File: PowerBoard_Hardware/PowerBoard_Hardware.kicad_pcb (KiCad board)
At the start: 4 copper layers, 279.4 x 127 mm, 152 parts, among them Q1 BSS138PW.115, Q10 Q_NMOS_GDS, Q11 Q_NMOS_GDS, Q12 Q_NMOS_GDS, Q13 Q_NMOS_GDS, Q2 BSS138PW.115, Q3 IPT020N10N3, Q4 IPT020N10N3, Q5 IPT020N10N3, Q6 Q_NMOS_GDS, Q7 Q_NMOS_GDS, Q8 Q_NMOS_GDS, Q9 Q_NMOS_GDS, U1 TM4C129E_Launchpad, U10 OKI, U11 LT1910, U12 LT1910, U13 LT1910, U14 LT1910, U15 ATC_FUSE_BLOCK, U16 ATC_FUSE_BLOCK, U17 ATC_FUSE_BLOCK, U18 ATC_FUSE_BLOCK, U19 ACS722xLCTR-40AU, U2 ATC_FUSE_BLOCK, U20 ACS722xLCTR-40AU, U21 ACS722xLCTR-40AU, U22 ACS722xLCTR-40AU, U23 LT1910, U24 LT1910, U25 LT1910, U26 LT1910, U27 ATC_FUSE_BLOCK, U28 ATC_FUSE_BLOCK, U29 ATC_FUSE_BLOCK, U3 ATC_FUSE_BLOCK, U30 ATC_FUSE_BLOCK, U31 ACS722xLCTR-40AU, U32 ACS722xLCTR-40AU, U33 ACS722xLCTR-40AU, U34 ACS722xLCTR-40AU, U4 ATC_FUSE_BLOCK, U5 LT1910, U6 LT1910, U7 ACS722xLCTR-40AU, U8 ACS722xLCTR-40AU, U9 ACS722xLCTR-40AU

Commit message: Moved Packages and Devices. Performed Basic Touch ups
Fixed some silkscreen and bad routing for a cleaner look. Moved the Packages and Devices to their own folder.
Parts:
- removed the Britt at (144.8, 55.9)
- removed the Carol at (196.8, 55.9)
- removed the G*** at (92.7, 48.9)
- added Britt: DC-DC_Converter, DC_DC_Converter_Quarter_Brick:DC_DC_Converter_Quarter_Brick, F.Cu at (144.8, 56.4)
- added Carol: DC-DC_Converter, DC_DC_Converter_Quarter_Brick:DC_DC_Converter_Quarter_Brick, F.Cu at (197.1, 55.4)
- added D14: D_Schottky, Diodes_SMD:D_0603, F.Cu at (105.4, 30.5)
- added G***: LOGO, MRDT-Silkscreen:MRDT_Logo_30mm, F.Cu at (118.4, 103.6)
- moved G*** 64.0 mm to (116.8, 89.9)
- moved D10 7.96 mm to (31.8, 103.5)
- moved D9 7.67 mm to (31.8, 120.0)
- moved D11 7.59 mm to (31.9, 87.0)
- moved D8 6.98 mm to (31.8, 138.4)
- moved D4 2.62 mm to (279.4, 50.8)
- moved D5 1.42 mm to (279.4, 125.7)
- moved D7 1.27 mm to (280.0, 101.0)
- moved D6 1.27 mm to (280.0, 74.3)
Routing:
- net +3.3VA: track 626.9 -> 646.8 mm, vias 14 -> 13
- net AUX_CTL: track 24.8 -> 7.21 mm
- net GND: track 231.2 -> 224.1 mm
- net COM_CTL: track 145.3 -> 139.1 mm
- net Net-(D8-Pad2): track 8.90 -> 4.10 mm
- net Net-(D11-Pad2): track 7.32 -> 2.61 mm
- net Net-(D9-Pad2): track 7.32 -> 3.32 mm
- net Net-(D10-Pad2): track 7.32 -> 3.95 mm
- net Net-(C29-Pad1): track 12.7 -> 16.0 mm
- net Net-(D4-Pad2): track 6.12 -> 3.32 mm
- net Net-(D5-Pad2): track 5.48 -> 3.95 mm
- net Net-(D7-Pad2): track 5.22 -> 3.95 mm
- net Net-(D6-Pad2): track 2.68 -> 3.95 mm
- net Net-(CONV1-Pad2): track 58.3 -> 59.3 mm
- net COM_IMEAS: track 124.1 -> 123.2 mm
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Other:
- board text added: "ACT"
- board text added: "COMM"
- board text added: "LOGIC"
- board text added: "Power Board Rev 1 2019 Mars Rover Design Team Missouri S&T Evan Hite"
- board text removed: "Actuation Bus"
- board text removed: "Communication Bus"
- board text removed: "Logic Bus"
- board text removed: "Power Board Rev 1 2019 Mars Rover Design Team Missouri University of Science and Technology Evan Hite"

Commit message: Corrected Vertical Anderson Package
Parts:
- removed Britt, Carol: DC-DC_Converter, DC_DC_Converter_Quarter_Brick:DC_DC_Converter_Quarter_Brick
- added CONV1: DC-DC_Converter, PowerBoard_Hardware:DC_DC_Converter_Quarter_Brick, F.Cu at (144.8, 56.4)
- added CONV2: DC-DC_Converter, PowerBoard_Hardware:DC_DC_Converter_Quarter_Brick, F.Cu at (197.1, 55.4)
- Conn1, Conn2, Conn3: footprint Vertical Anderson Double:Vertical Anderson Double -> PowerBoard_Hardware:Vertical_Anderson_Double_SidebySide
- moved Conn1 41.4 mm to (263.5, -10.8)
- moved Conn2 39.1 mm to (179.3, -8.51)
- moved Conn3 38.8 mm to (223.9, -8.26)

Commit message: Corrected Vertical Anderson Package and Replaced on Layout
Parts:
- moved Conn1 24.5 mm to (267.0, 13.5)
- moved Conn2 22.0 mm to (180.6, 13.5)
- moved Conn3 21.7 mm to (223.8, 13.5)
- moved D1 0.76 mm to (263.7, 17.8)
- moved R7 0.76 mm to (263.7, 23.3)
- moved REF** 0.25 mm to (279.7, 17.1)
- moved REF** 0.25 mm to (279.7, 83.8)

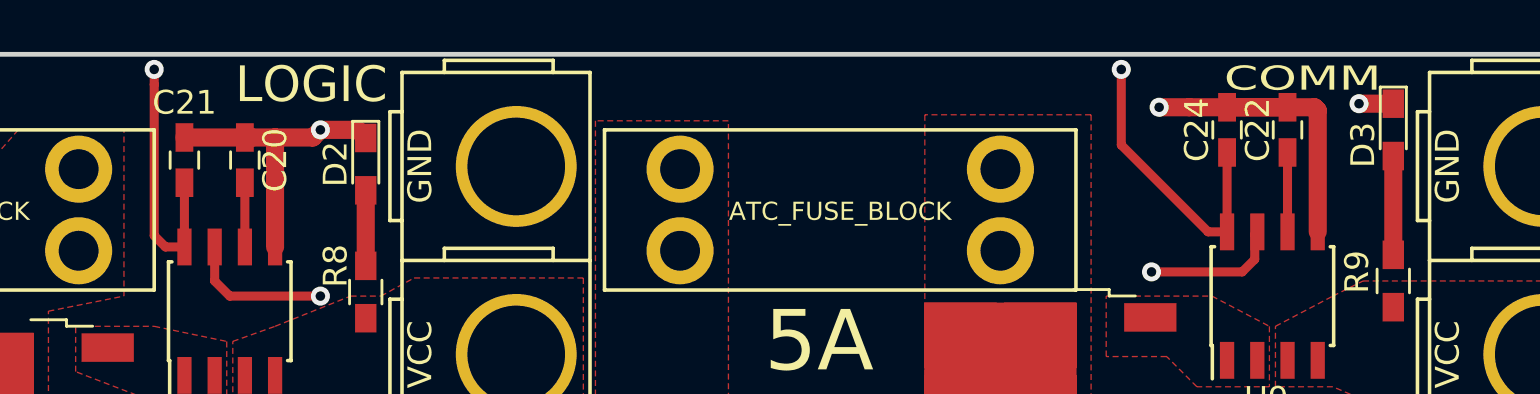
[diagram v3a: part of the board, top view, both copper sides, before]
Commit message: Swapped Placment of Comm & Logic Busses
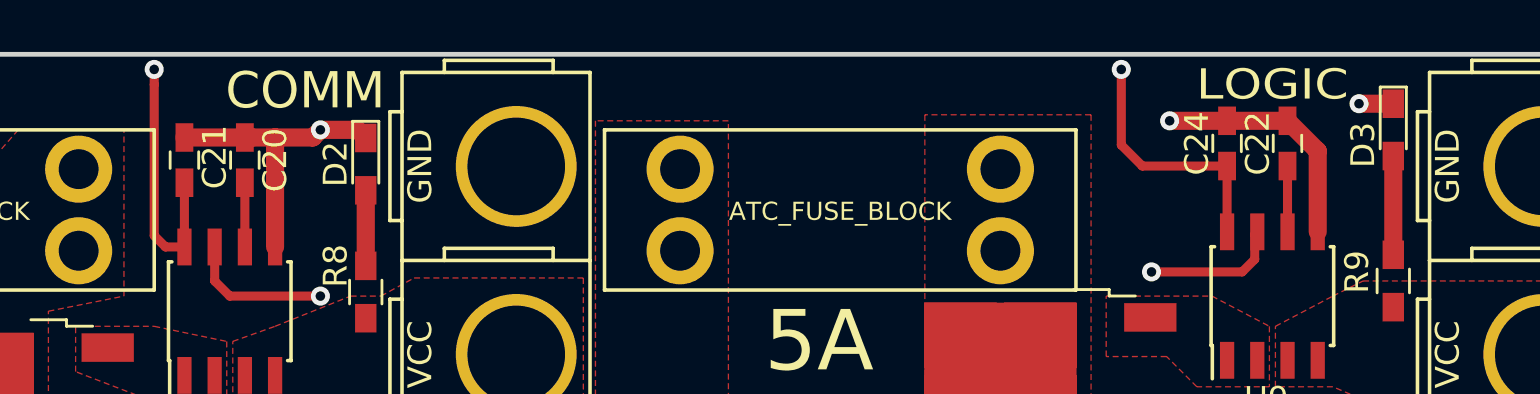
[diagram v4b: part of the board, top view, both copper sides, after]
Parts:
- moved C22 0.57 mm to (217.8, 16.4)
- moved C24 0.57 mm to (215.3, 16.4)
- turned C21 to 90 degrees
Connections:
- C21 pad 1: GND -> +3.3VA
- C21 pad 2: +3.3VA -> GND
- U1 pad PD1: COM_CTL -> LOGIC_CTL
- U1 pad PE0: LOGIC_IMEAS -> COM_IMEAS
- U1 pad PE1: COM_IMEAS -> LOGIC_IMEAS
- U1 pad PH2: LOGIC_CTL -> COM_CTL
- U5 pad 4: LOGIC_CTL -> COM_CTL
- U6 pad 4: COM_CTL -> LOGIC_CTL
- U7 pad 7: LOGIC_IMEAS -> COM_IMEAS
- U9 pad 7: COM_IMEAS -> LOGIC_IMEAS
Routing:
- net LOGIC_CTL: track 94.5 -> 139.1 mm, vias 1 -> 3
- net COM_CTL: track 139.1 -> 94.5 mm, vias 3 -> 1
- net LOGIC_IMEAS: track 90.4 -> 123.2 mm
- net COM_IMEAS: track 123.2 -> 90.4 mm
- net GND: track 224.1 -> 219.9 mm
- net +3.3VA: track 646.8 -> 645.0 mm
- net Net-(C22-Pad1): track 3.34 -> 2.77 mm

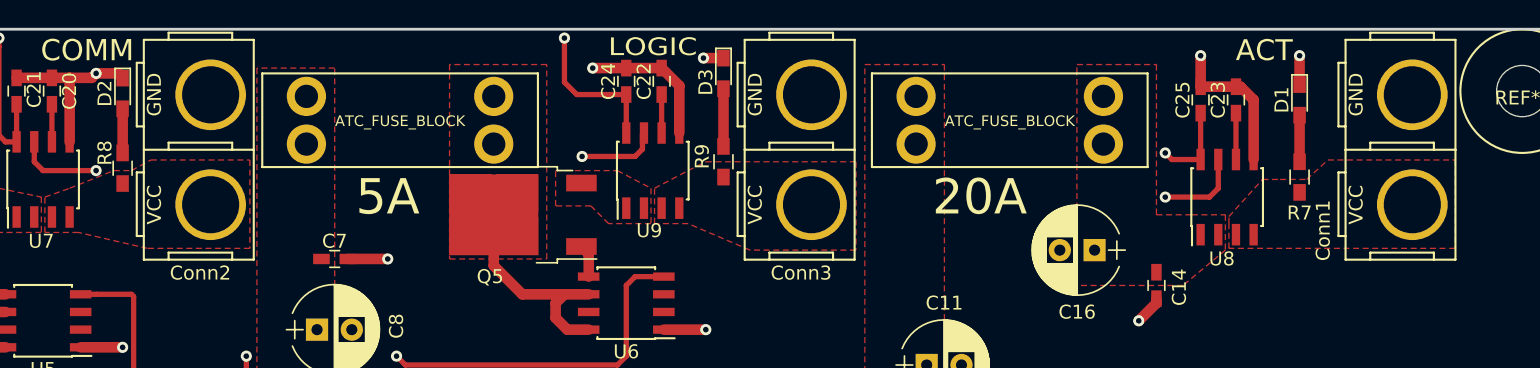
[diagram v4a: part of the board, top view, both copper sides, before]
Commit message: Adjusted connector placement
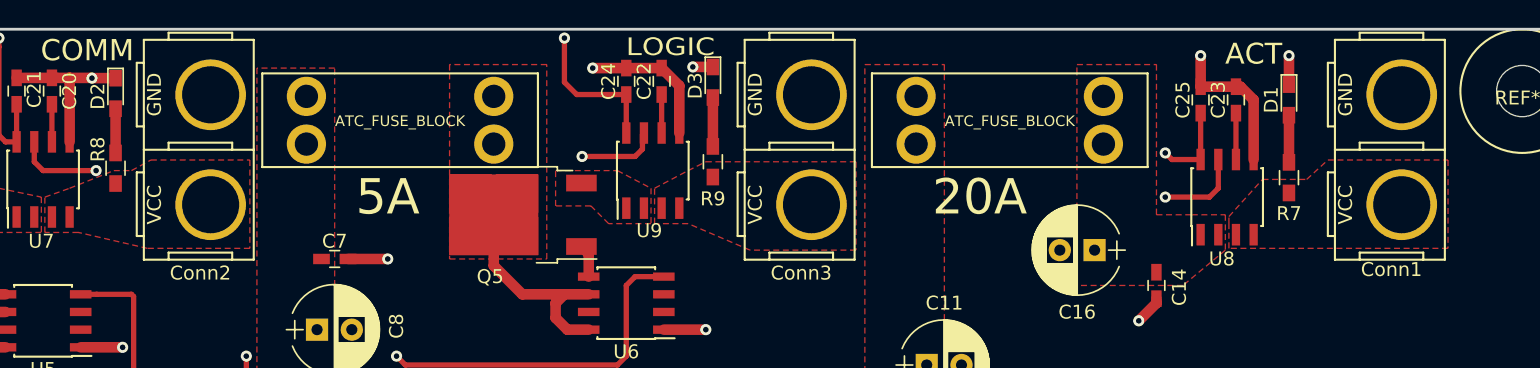
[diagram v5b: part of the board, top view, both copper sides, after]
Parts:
- moved D3 0.99 mm to (221.5, 16.5)
- moved R7 0.76 mm to (262.9, 23.4)
- moved Conn1 0.76 mm to (266.2, 13.5)
- moved D1 0.76 mm to (262.9, 17.8)
- moved R9 0.76 mm to (221.5, 22.2)
- moved D2 0.51 mm to (178.6, 17.3)
- moved R8 0.51 mm to (178.6, 22.7)
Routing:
- net GND: track 219.9 -> 219.2 mm
- net Net-(D3-Pad2): track 4.15 -> 3.52 mm

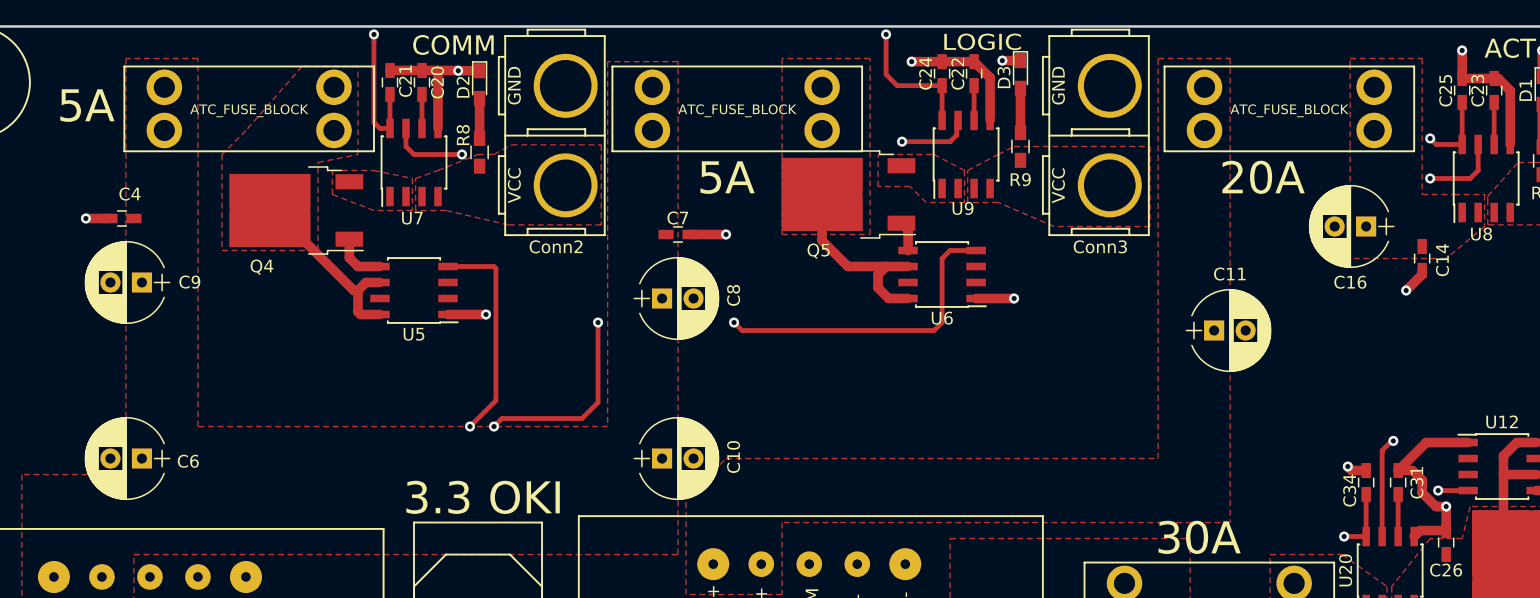
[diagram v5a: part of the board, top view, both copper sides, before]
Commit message: Added a BOM and Updated Capacitor Size
Added a BOM file in the Documentation file. Currently has 2 placeholder values in it due to unknown anderson powerpole colors. Updated the 330u capacitor package to fit a real capacitor.
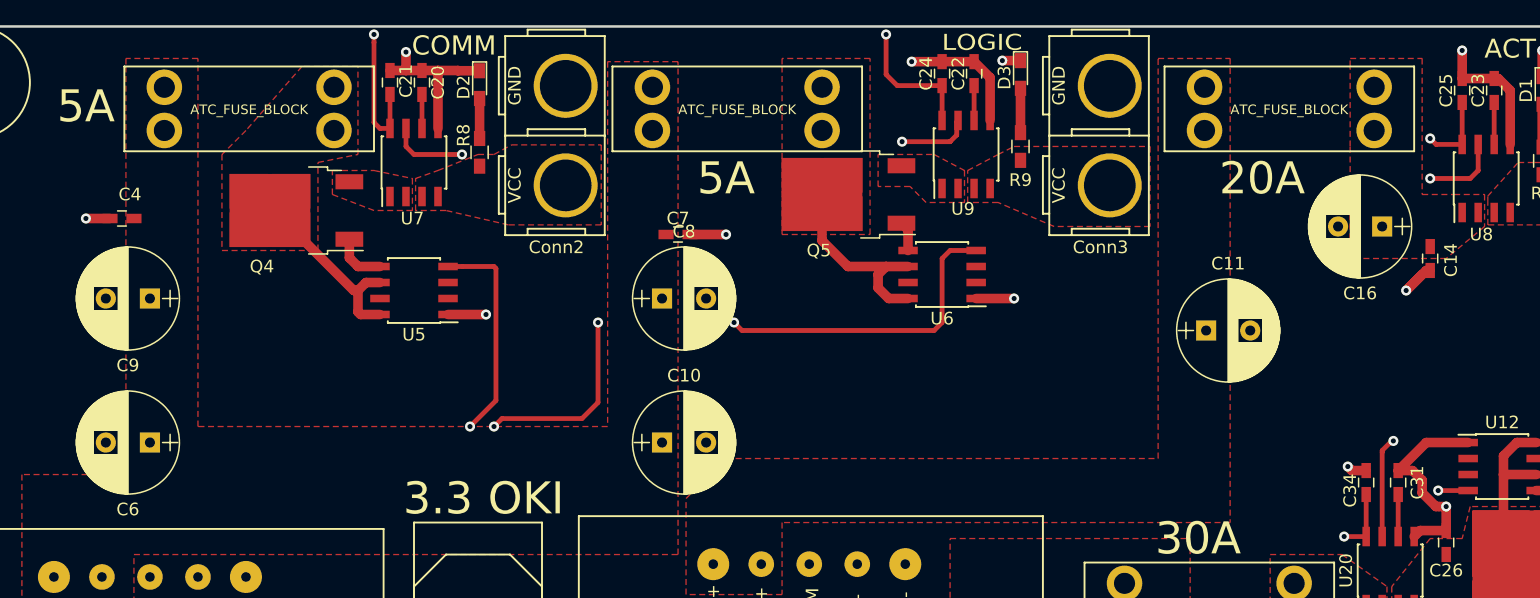
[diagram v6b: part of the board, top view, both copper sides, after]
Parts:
- C10, C11, C16, C6, C8, C9: footprint Capacitors_THT:CP_Radial_D6.3mm_P2.50mm -> Capacitors_THT:CP_Radial_D8.0mm_P3.50mm
- C26: value 0.1 -> 0.1u
- moved C6 1.42 mm to (152.4, 45.7)
- moved C9 1.42 mm to (152.4, 34.3)
- moved C16 1.27 mm to (250.2, 28.6)
- moved C10 1.27 mm to (193.0, 45.7)
- moved C11 0.63 mm to (236.2, 36.8)
- moved C14 0.63 mm to (254.0, 31.1)
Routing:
- net GND: track 219.2 -> 222.9 mm

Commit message: Created Gerbs
Created the Gerber files. Had to adjust the edgecuts to get the file to be able to be created.
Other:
- board size 279.4 x 127 mm -> 279.4 x 126.9 mm
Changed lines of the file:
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@@
   (general
     (thickness 1.6)
-    (drawings 49)
+    (drawings 48)
     (tracks 897)
     (zones 0)
@@
     (47 F.CrtYd user)
     (48 B.Fab user)
-    (49 F.Fab user hide)
+    (49 F.Fab user)
   )
   (setup
-    (last_trace_width 0.762)
+    (last_trace_width 0.25)
     (user_trace_width 0.254)
     (user_trace_width 0.381)
@@
       (outputformat 1)
       (mirror false)
-      (drillshape 1)
+      (drillshape 0)
       (scaleselection 1)
       (outputdirectory ""))
@@
     )
   )
+  (gr_line (start 292.1 16.81) (end 292.07 135.34) (layer Edge.Cuts) (width 0.2))
+  (gr_arc (start 16.6624 16.6624) (end 16.7386 12.7) (angle -92.6) (layer Edge.Cuts) (width 0.2))
   (gr_text - (at 29.464 44.45) (layer F.SilkS)
     (effects (font (size 1.524 1.524) (thickness 0.381)))
@@
     (effects (font (size 12.7 12.7) (thickness 1.27)))
   )
-  (gr_arc (start 16.637 16.637) (end 16.637 12.7) (angle -90) (layer Edge.Cuts) (width 0.2))
-  (gr_arc (start 16.764 135.636) (end 12.7 135.636) (angle -90) (layer Edge.Cuts) (width 0.2))
-  (gr_arc (start 288.036131 135.640092) (end 287.909132 139.704091) (angle -93.63749996) (layer Edge.Cuts) (width 0.2))
-  (gr_arc (start 288.1376 16.6624) (end 292.1 16.6624) (angle -89.24615167) (layer Edge.Cuts) (width 0.2))
-  (gr_circle (center 288.1376 16.637) (end 288.1122 16.5354) (layer Edge.Cuts) (width 0.2))
+  (gr_arc (start 16.599284 135.640593) (end 12.7 135.636) (angle -90.97528799) (layer Edge.Cuts) (width 0.2))
+  (gr_arc (start 288.010731 135.513092) (end 287.8836 139.573) (angle -94.10571235) (layer Edge.Cuts) (width 0.2))
+  (gr_arc (start 288.1376 16.6624) (end 292.1 16.77) (angle -87.7888971) (layer Edge.Cuts) (width 0.2))
   (gr_text "Power Board Rev 1 2019\nMars Rover Design Team\nMissouri S&T\nEvan Hite" (at 114.808 83.312) (layer F.SilkS)
     (effects (font (size 1.5 1.5) (thickness 0.3)))
@@
     (effects (font (size 1.5 1.5) (thickness 0.3)))
   )
-  (gr_line (start 292.1 135.509) (end 292.1 16.51) (layer Edge.Cuts) (width 0.2))
-  (gr_line (start 288.036 139.7) (end 80.01 139.7) (layer Edge.Cuts) (width 0.2))
-  (gr_line (start 288.29 12.7) (end 16.51 12.7) (layer Edge.Cuts) (width 0.2))
-  (gr_line (start 12.7 16.637) (end 12.7 135.636) (layer Edge.Cuts) (width 0.2))
+  (gr_line (start 287.909 139.573) (end 79.9846 139.573) (layer Edge.Cuts) (width 0.2))
+  (gr_line (start 288.417 12.7) (end 16.7386 12.7) (layer Edge.Cuts) (width 0.2))
+  (gr_line (start 12.7 16.79) (end 12.7 135.636) (layer Edge.Cuts) (width 0.2))
   (gr_line (start 133.35 17.78) (end 133.35 19.05) (layer F.SilkS) (width 0.2))
   (gr_line (start 15.24 17.78) (end 133.35 17.78) (layer F.SilkS) (width 0.2))
@@
   (gr_line (start 15.24 19.05) (end 15.24 17.78) (layer F.SilkS) (width 0.2))
   (gr_line (start 15.24 73.66) (end 15.24 19.05) (layer F.SilkS) (width 0.2))
-  (gr_line (start 16.764 139.7) (end 80.01 139.7) (layer Edge.Cuts) (width 0.2))
+  (gr_line (start 16.65 139.54) (end 79.99 139.57) (layer Edge.Cuts) (width 0.2))
   (segment (start 27.94 43.18) (end 34.23 43.18) (width 0.381) (layer F.Cu) (net 1))
   (segment (start 26.67 44.45) (end 27.94 43.18) (width 0.381) (layer F.Cu) (net 1))

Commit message: Updated Gerbs and Updated BOM
Basic Updates to make the BOM more legible. Also the Layout and Schematic were updated for easier reading and a new Gerbs was generated to reflect this.
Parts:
- CONV1, CONV2: footprint PowerBoard_Hardware:DC_DC_Converter_Quarter_Brick -> PowerBoard_Hardware2:DC_DC_Converter_Quarter_Brick
- moved REF** 0.16 mm to (12.7, 139.5)
- moved REF** 0.14 mm to (292.0, 139.6)
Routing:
- net +3.3VA: track 645.0 -> 650.8 mm
- net Net-(CONV2-Pad2): track 110.7 -> 109.3 mm
